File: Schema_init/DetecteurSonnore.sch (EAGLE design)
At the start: 13 parts, among them Q1 2N2222, Q2 2N2222

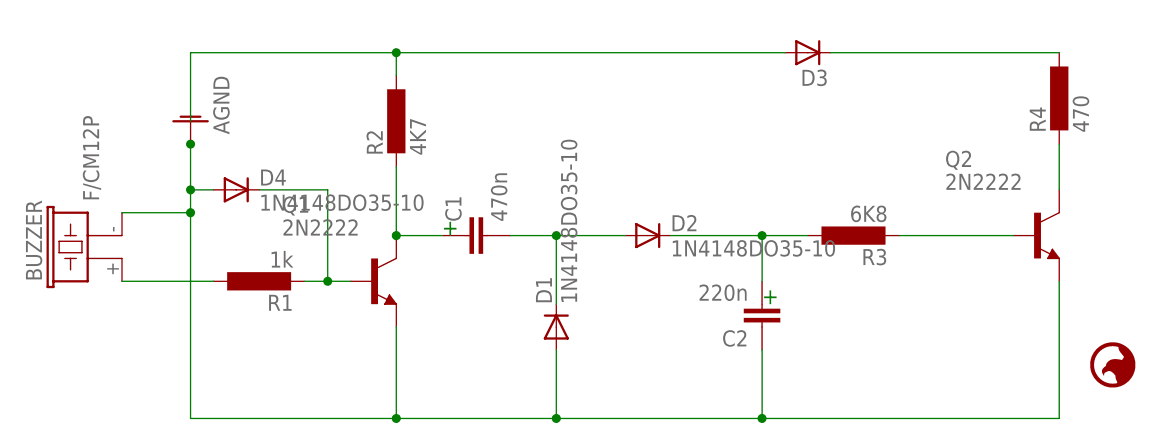
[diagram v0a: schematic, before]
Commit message: Ajout chapter 2 Breadboard, chapter 3 Eagle
A continuer évidemment mais c’est un premier jet!
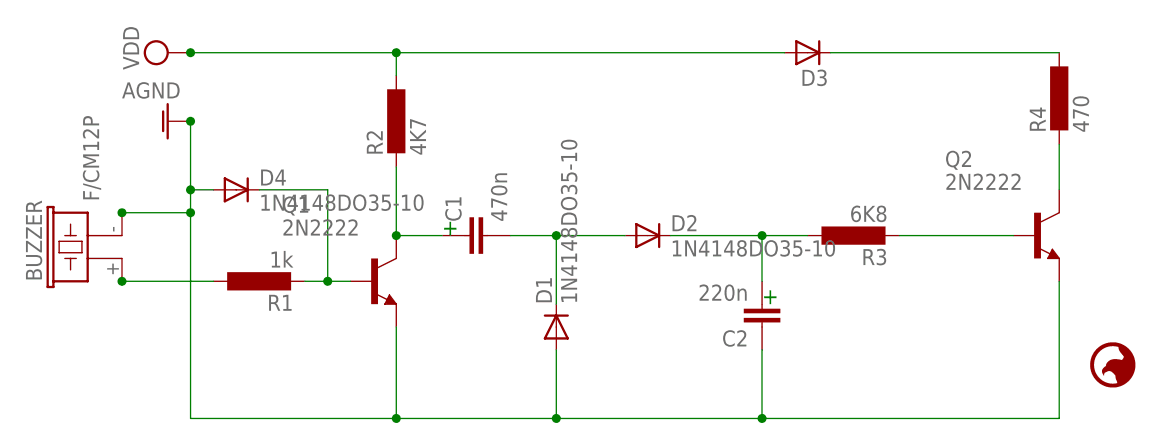
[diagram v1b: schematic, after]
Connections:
- net N$11 renamed VDD
- net AGND: now also BUZZER.2
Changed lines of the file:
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@@
 <part name="BUZZER" library="buzzer" deviceset="F/CM12P" device=""/>
 <part name="AGND1" library="supply1" deviceset="AGND" device=""/>
+<part name="SUPPLY1" library="supply2" deviceset="VDD" device=""/>
 </parts>
 <sheets>
@@
 <instance part="D3" gate="G$1" x="83.82" y="76.2" rot="R90"/>
 <instance part="BUZZER" gate="G$1" x="5.08" y="53.34" rot="R90"/>
-<instance part="AGND1" gate="VR1" x="15.24" y="68.58" rot="R180"/>
+<instance part="AGND1" gate="VR1" x="12.7" y="68.58" rot="R270"/>
+<instance part="SUPPLY1" gate="G$1" x="12.7" y="76.2" rot="R90"/>
 </instances>
 <busses>
@@
 </segment>
 </net>
-<net name="N$11" class="0">
-<segment>
-<pinref part="R2" gate="G$1" pin="1"/>
-<pinref part="D3" gate="G$1" pin="C"/>
-<wire x1="38.1" y1="73.66" x2="38.1" y2="76.2" width="0.1524" layer="91"/>
-<wire x1="38.1" y1="76.2" x2="81.28" y2="76.2" width="0.1524" layer="91"/>
-<wire x1="38.1" y1="76.2" x2="15.24" y2="76.2" width="0.1524" layer="91"/>
-<junction x="38.1" y="76.2"/>
-<wire x1="15.24" y1="76.2" x2="15.24" y2="68.58" width="0.1524" layer="91"/>
-</segment>
-</net>
 <net name="N$1" class="0">
 <segment>
@@
 <pinref part="R1" gate="G$1" pin="1"/>
 <wire x1="7.62" y1="50.8" x2="17.78" y2="50.8" width="0.1524" layer="91"/>
+<junction x="7.62" y="50.8"/>
 </segment>
 </net>
@@
 <pinref part="D4" gate="G$1" pin="A"/>
 <wire x1="17.78" y1="60.96" x2="15.24" y2="60.96" width="0.1524" layer="91"/>
-<wire x1="15.24" y1="60.96" x2="15.24" y2="66.04" width="0.1524" layer="91"/>
+<wire x1="15.24" y1="60.96" x2="15.24" y2="68.58" width="0.1524" layer="91"/>
 <wire x1="15.24" y1="35.56" x2="38.1" y2="35.56" width="0.1524" layer="91"/>
 <pinref part="Q2" gate="G$1" pin="E"/>
@@
 <junction x="15.24" y="58.42"/>
 <pinref part="AGND1" gate="VR1" pin="AGND"/>
-<junction x="15.24" y="66.04"/>
+<junction x="15.24" y="68.58"/>
+<pinref part="BUZZER" gate="G$1" pin="2"/>
+<junction x="7.62" y="58.42"/>
 </segment>
 </net>
+<net name="VDD" class="0">
+<segment>
+<pinref part="R2" gate="G$1" pin="1"/>
+<pinref part="D3" gate="G$1" pin="C"/>
+<wire x1="38.1" y1="73.66" x2="38.1" y2="76.2" width="0.1524" layer="91"/>
+<wire x1="38.1" y1="76.2" x2="81.28" y2="76.2" width="0.1524" layer="91"/>
+<wire x1="38.1" y1="76.2" x2="15.24" y2="76.2" width="0.1524" layer="91"/>
+<junction x="38.1" y="76.2"/>
+<pinref part="SUPPLY1" gate="G$1" pin="VDD"/>
+<junction x="15.24" y="76.2"/>
+</segment>
+</net>
